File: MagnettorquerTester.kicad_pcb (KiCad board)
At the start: 2 copper layers, 86 x 86 mm, 156 parts, among them J1 Out Conn 1, J2 Out Conn 2, J3 Out Conn 3, J4 Out Conn 4, J5 In Conn, J6 USB-C Receptacle, Q1 BSS138, SW1 Reset, SW2 BOOTSEL, U1 LIS3MDL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

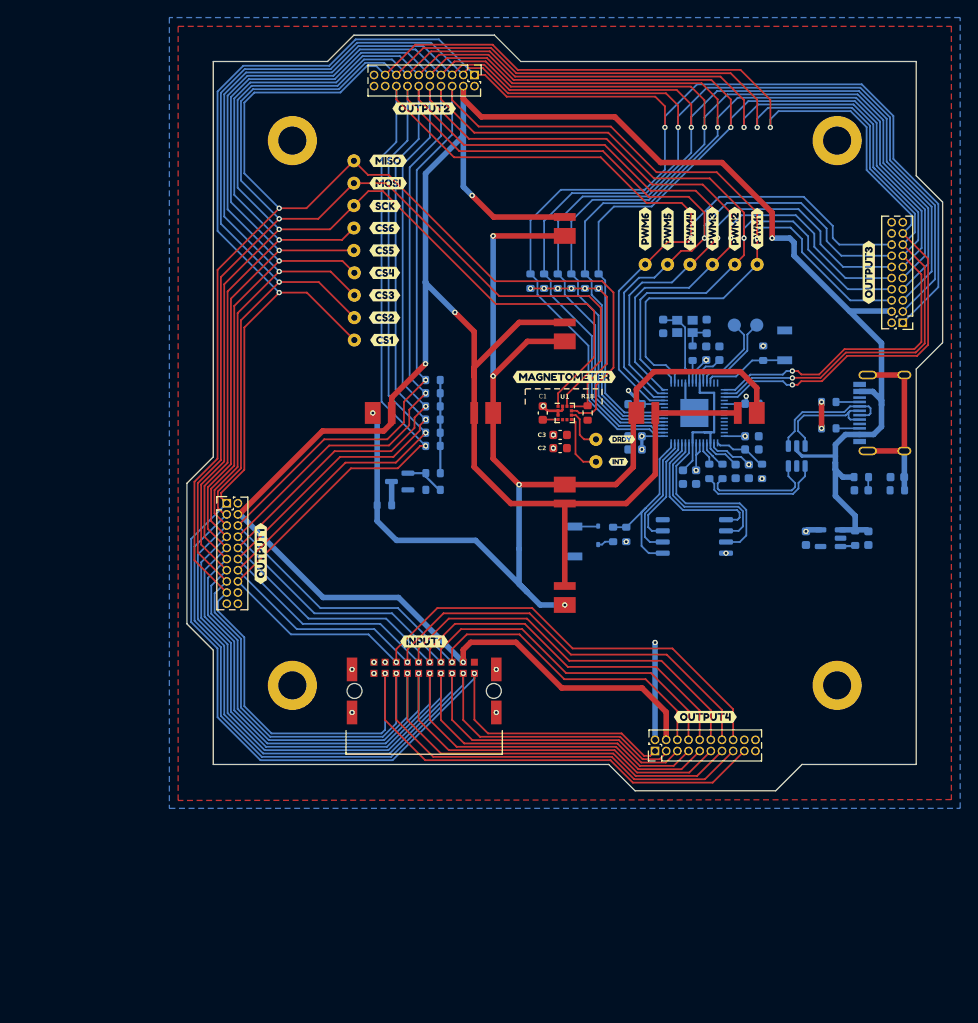
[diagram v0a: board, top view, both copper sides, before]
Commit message: Exported BOM
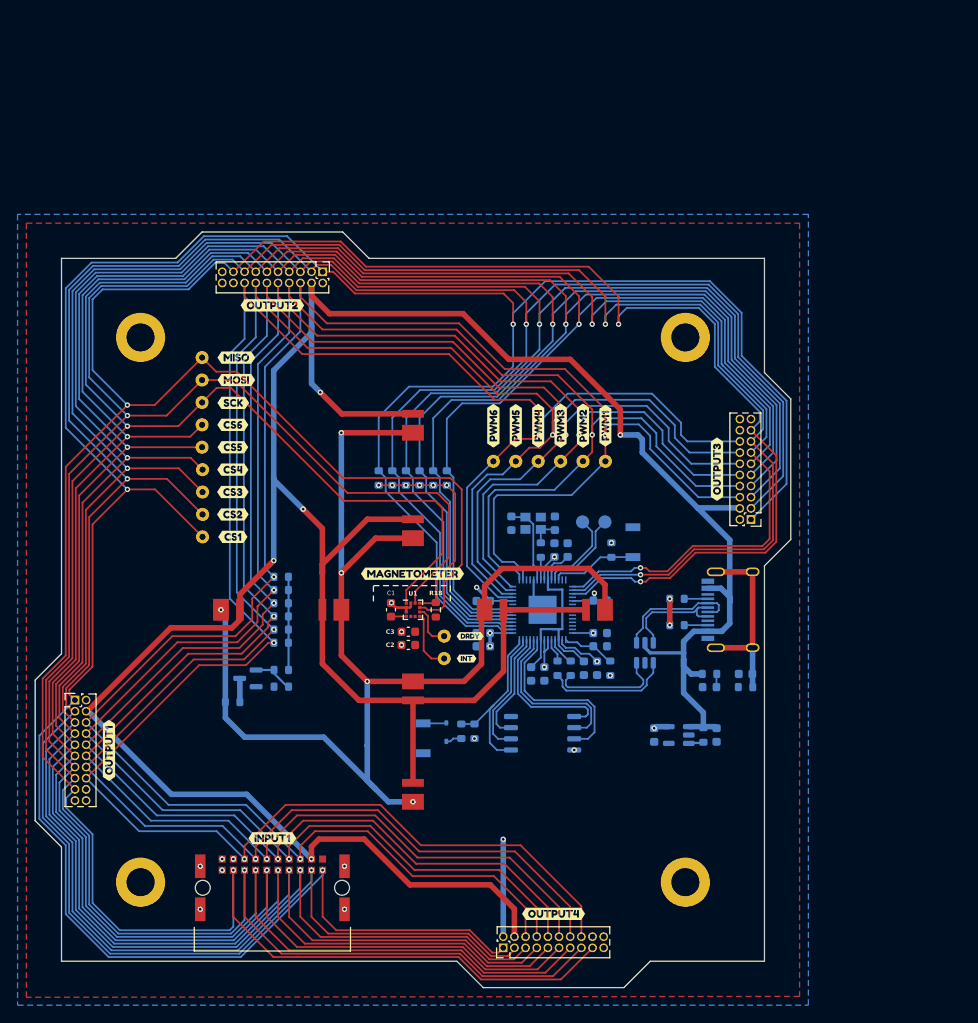
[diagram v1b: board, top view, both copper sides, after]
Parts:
- moved C1 28.3 mm to (155.2, 94.4)
- moved C10 28.3 mm to (165.7, 93.4)
- moved C18 28.3 mm to (195.6, 101.7)
- moved C19 28.3 mm to (192.3, 108.7)
- moved C2 28.3 mm to (157.2, 98.4)
- moved C3 28.3 mm to (157.2, 96.9)
- moved D1 28.3 mm to (157.7, 73.4)
- moved D10 28.3 mm to (191.5, 103.2)
- moved D11 28.3 mm to (161.5, 108.3)
- moved D2 28.3 mm to (178.7, 94.4)
- moved D3 28.3 mm to (157.7, 115.4)
- moved D4 28.3 mm to (136.7, 94.4)
- moved D5 28.3 mm to (157.7, 85.4)
- moved D6 28.3 mm to (166.7, 94.4)
- moved D7 28.3 mm to (157.7, 103.4)
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
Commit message: Added slots for USB cables
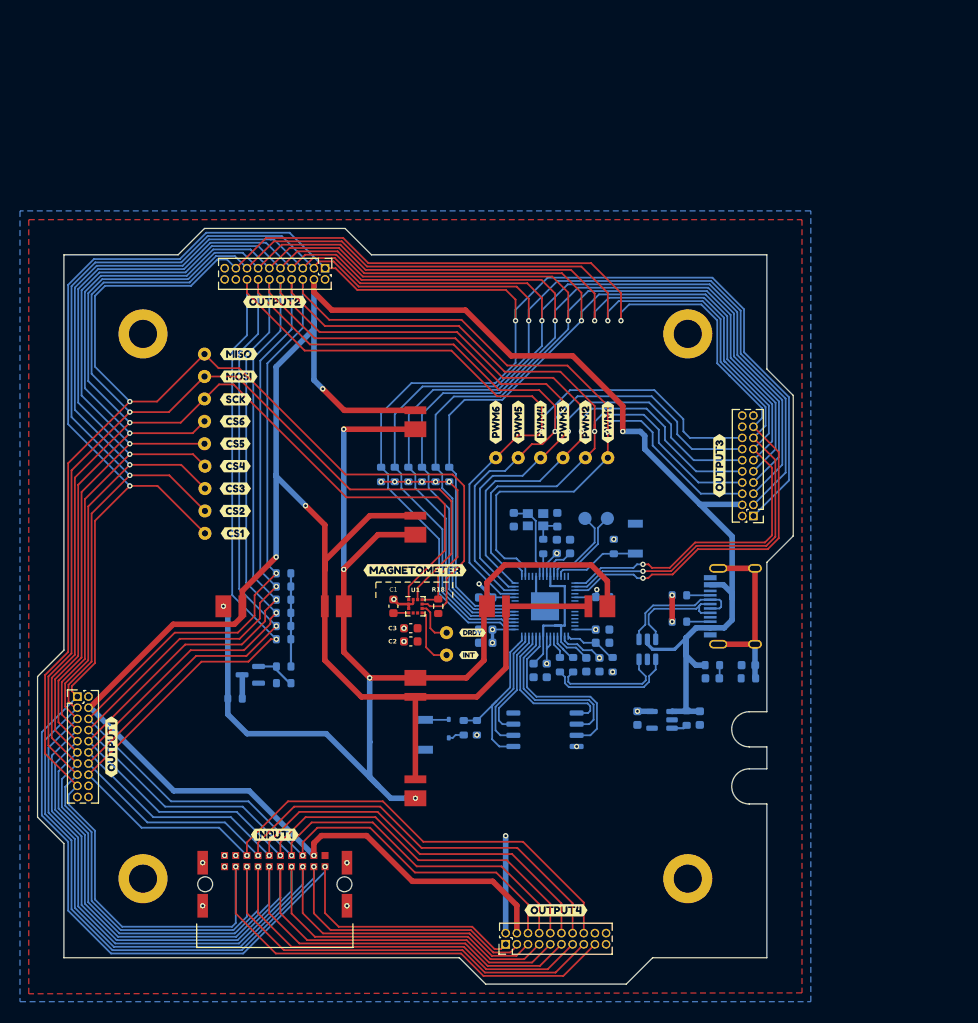
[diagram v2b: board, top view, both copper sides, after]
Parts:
- moved C19 2.71 mm to (190.4, 106.7)
- moved C20 2.71 mm to (183.3, 106.7)
- moved R28 2.71 mm to (188.9, 106.7)
- moved U5 2.57 mm to (186.1, 106.9)
- moved C18 1.05 mm to (195.9, 100.7)
- moved D10 1.05 mm to (191.8, 102.2)
- moved R22 1.05 mm to (195.9, 102.2)
- moved R26 1.05 mm to (191.8, 100.7)
- moved C1 0.49 mm to (155.5, 94.0)
- moved C10 0.49 mm to (166.0, 93.0)
- moved C2 0.49 mm to (157.5, 98.0)
- moved C3 0.49 mm to (157.5, 96.5)
- moved D1 0.49 mm to (158.0, 73.0)
- moved D11 0.49 mm to (161.8, 107.9)
- moved D2 0.49 mm to (179.0, 94.0)
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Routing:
- net VBUS: track 342.8 -> 342.2 mm
- net Net-(J6-SHIELD): track 21.5 -> 20.9 mm
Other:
- outline, holes or cut-outs redrawn

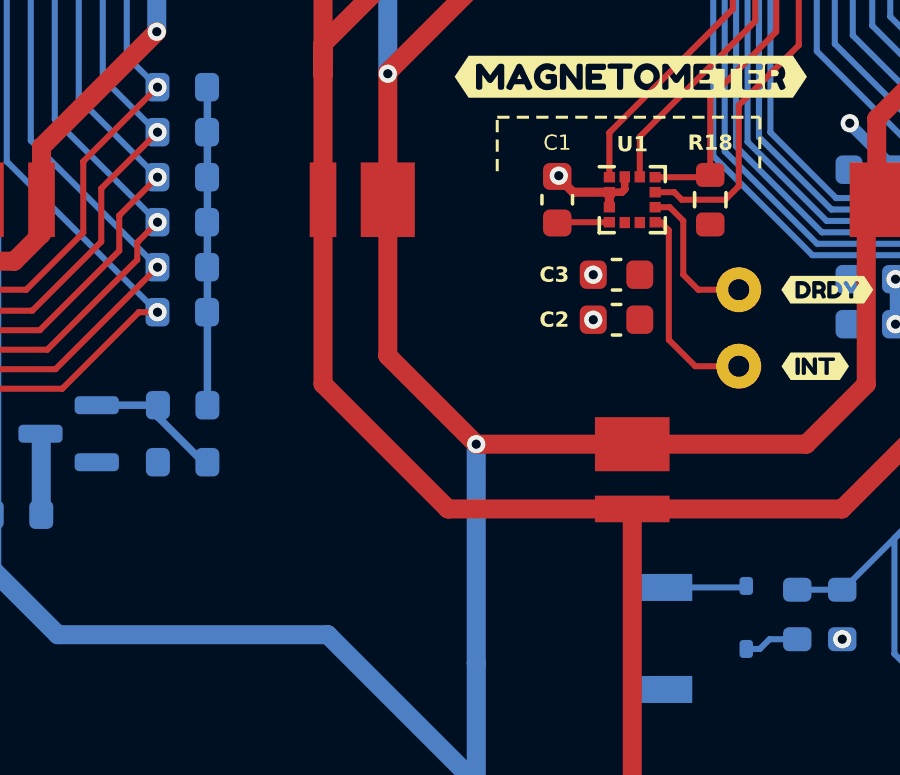
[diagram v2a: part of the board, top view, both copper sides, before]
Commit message: Some silkscreen stuff
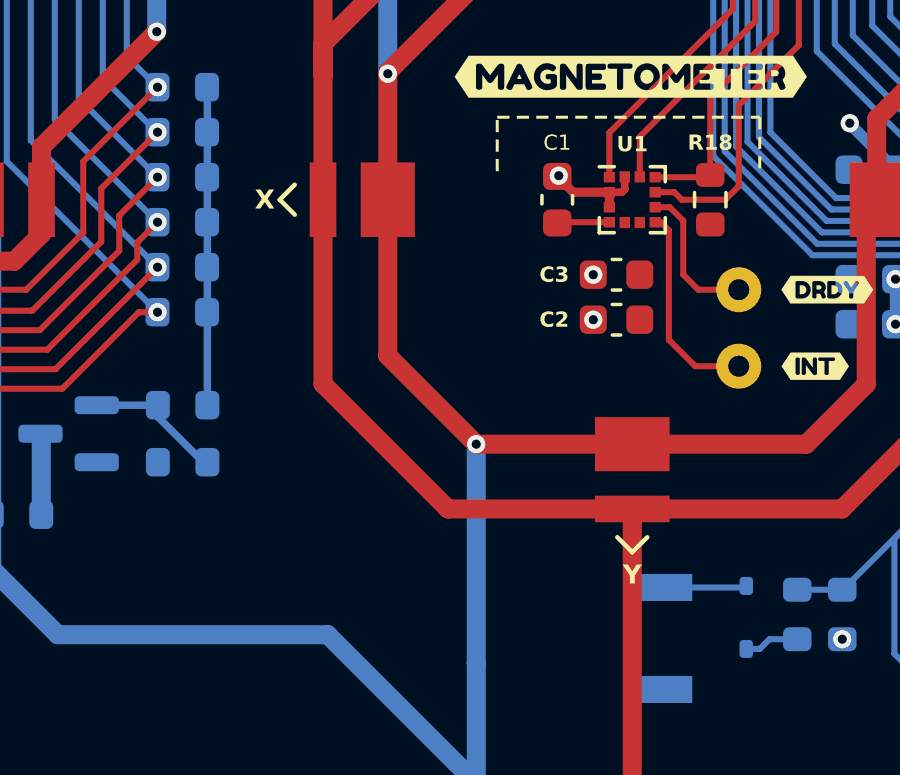
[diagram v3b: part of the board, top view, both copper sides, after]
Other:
- board text added: "X"
- board text added: "Y"
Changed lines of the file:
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@@
   (gr_line (start 153.5 91.25) (end 162.25 91.25)
     (stroke (width 0.1016) (type dash)) (layer "F.SilkS"))
+  (gr_line (start 158 105.75) (end 157.5 105.25)
+    (stroke (width 0.15) (type default)) (layer "F.SilkS"))
+  (gr_line (start 146.25 94) (end 146.75 94.5)
+    (stroke (width 0.15) (type default)) (layer "F.SilkS"))
+  (gr_line (start 146.25 94) (end 146.75 93.5)
+    (stroke (width 0.15) (type default)) (layer "F.SilkS"))
   (gr_line (start 162.25 91.25) (end 162.25 93.05)
     (stroke (width 0.1016) (type dash)) (layer "F.SilkS"))
+  (gr_line (start 158 105.75) (end 158.5 105.25)
+    (stroke (width 0.15) (type default)) (layer "F.SilkS"))
   (gr_line (start 153.5 93.05) (end 153.5 91.25)
     (stroke (width 0.1016) (type dash)) (layer "F.SilkS"))
@@
   (gr_line (start 182 137) (end 185 134)
     (stroke (width 0.1) (type default)) (layer "Edge.Cuts"))
+  (gr_text "X" (at 145.75 94) (layer "F.SilkS")
+    (effects (font (size 0.635 0.635) (thickness 0.127) bold))
+  )
+  (gr_text "Y" (at 158 106.5) (layer "F.SilkS")
+    (effects (font (size 0.635 0.635) (thickness 0.127) bold))
+  )
   (gr_text "Rev A" (at 157.525 59.6) (layer "B.Mask")
     (effects (font (size 0.635 0.635) (thickness 0.1524) bold) (justify left bottom mirror))
@@
     (pts (xy 118 54) (xy 118 134))
     (height 9.025)
-    (gr_text "80.0000 mm" (at 107.825 94 90) (layer "Dwgs.User")
+    (gr_text "3149.6063 mils" (at 107.825 94 90) (layer "Dwgs.User")
       (effects (font (size 1 1) (thickness 0.15)))
     )
@@
     (pts (xy 118 54) (xy 198 54))
     (height -8.8)
-    (gr_text "80.0000 mm" (at 158 44.05) (layer "Dwgs.User")
+    (gr_text "3149.6063 mils" (at 158 44.05) (layer "Dwgs.User")
       (effects (font (size 1 1) (thickness 0.15)))
     )
